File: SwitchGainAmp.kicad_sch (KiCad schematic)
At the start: 18 parts, among them Q3 BSS138, Q4 BSS138, Q5 BSS138, Q6 BSS138, U8 LT1493

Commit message: added company to all schematic pages
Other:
- company: (none) -> Jochen Steinmann
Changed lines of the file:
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@@
 (kicad_sch (version 20211123) (generator eeschema)
   (paper "A4")
+  (title_block
+    (rev "2")
+    (company "Jochen Steinmann")
+  )
   (junction (at 92.964 88.392) (diameter 0) (color 0 0 0 0)
   )

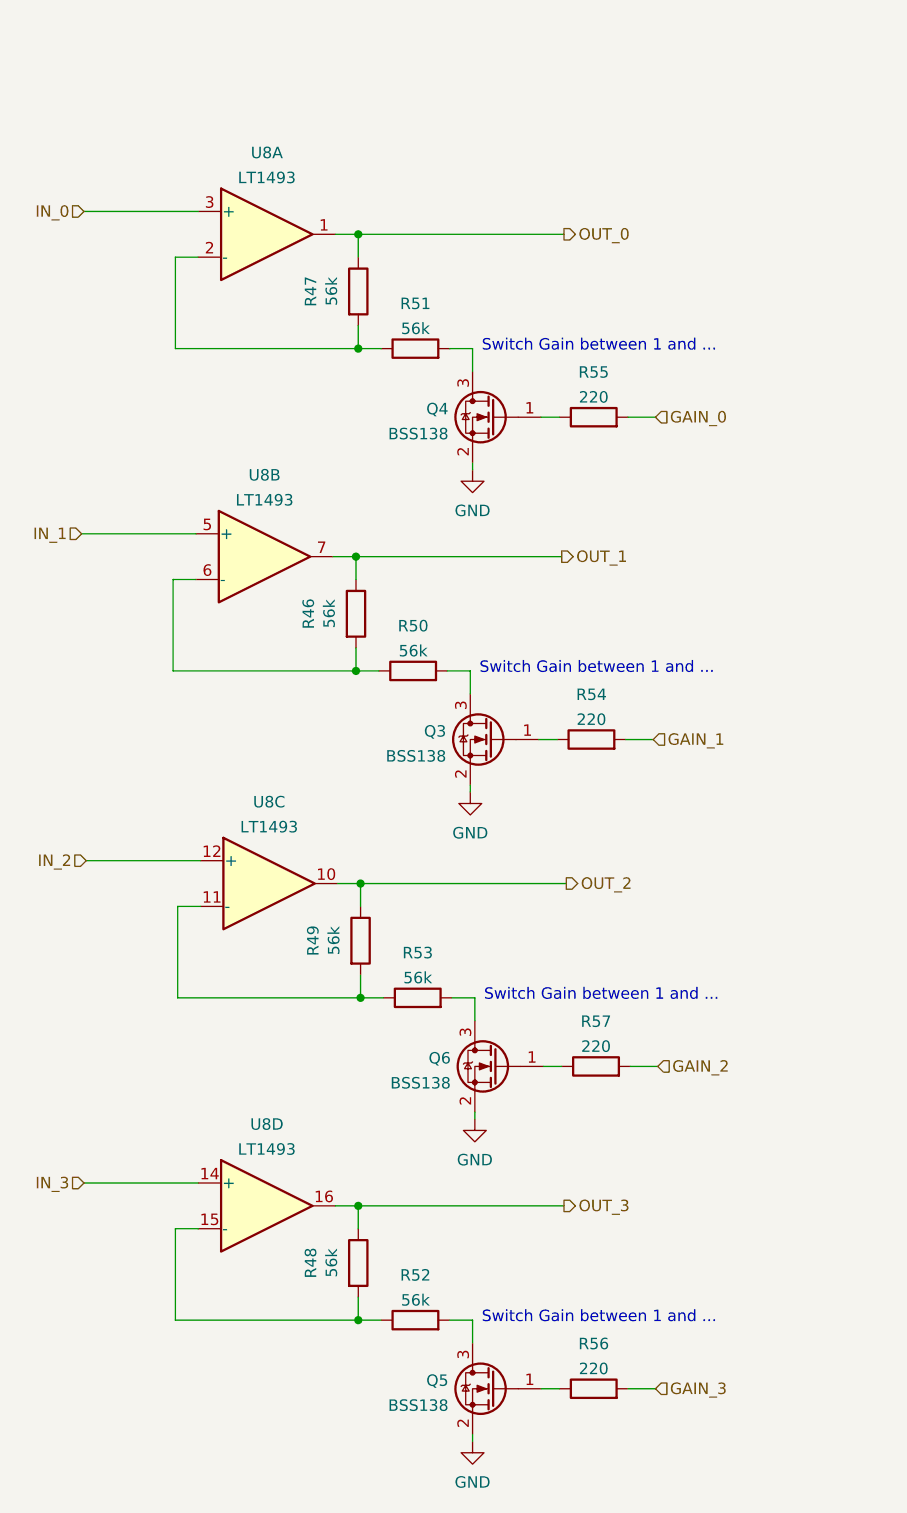
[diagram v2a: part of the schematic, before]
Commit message: added resistors at the amplifier output
these can decouple the filter / averaging capacitors from the op amp output and hence prevent ringing, oscillation.
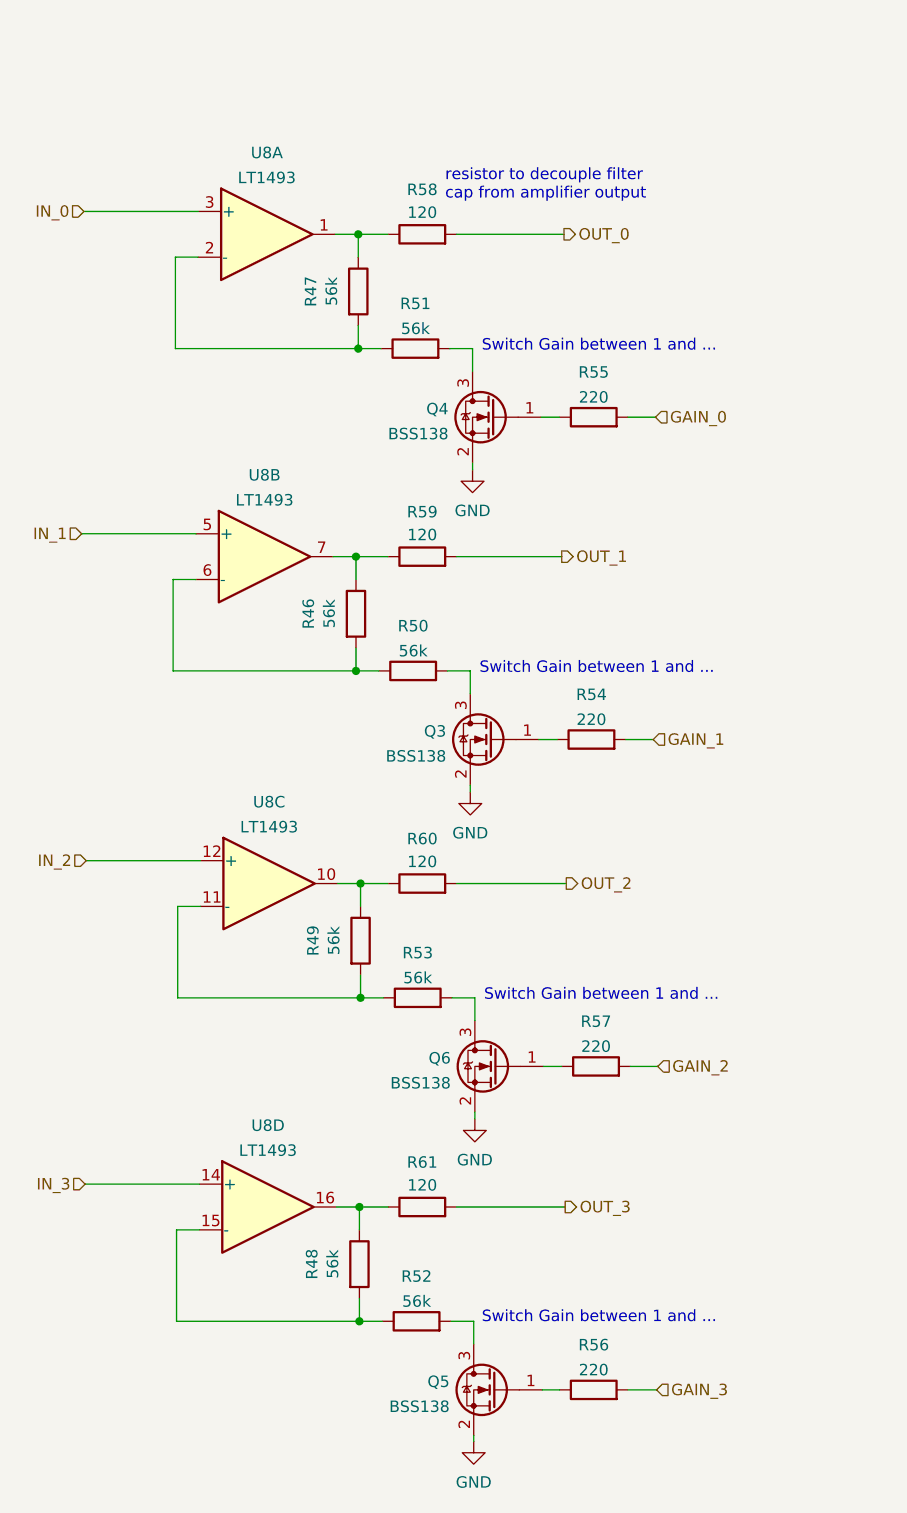
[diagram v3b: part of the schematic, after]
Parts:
- added R58, R59, R60, R61: 120, Resistor_SMD:R_0603_1608Metric, symbol Device:R
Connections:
- net OUT_0: now also R58.2; no longer R47.1, U8.1
- net OUT_1: now also R59.2; no longer R46.1, U8.7
- net OUT_2: now also R60.2; no longer R49.1, U8.10
- net OUT_3: now also R61.2; no longer R48.1, U8.16
- new net: R47.1, R58.1, U8.1
- new net: R48.1, R61.1, U8.16
- new net: R46.1, R59.1, U8.7
- new net: R49.1, R60.1, U8.10
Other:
- note added: "resistor to decouple filter cap from amplifier output"
